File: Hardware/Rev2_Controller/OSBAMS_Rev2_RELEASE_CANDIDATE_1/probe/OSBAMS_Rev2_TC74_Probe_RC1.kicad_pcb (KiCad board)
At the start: 2 copper layers, 30 x 18 mm, 5 parts, among them J1 TO_CONTROLLER, U1 TC74A5-3.3VAT

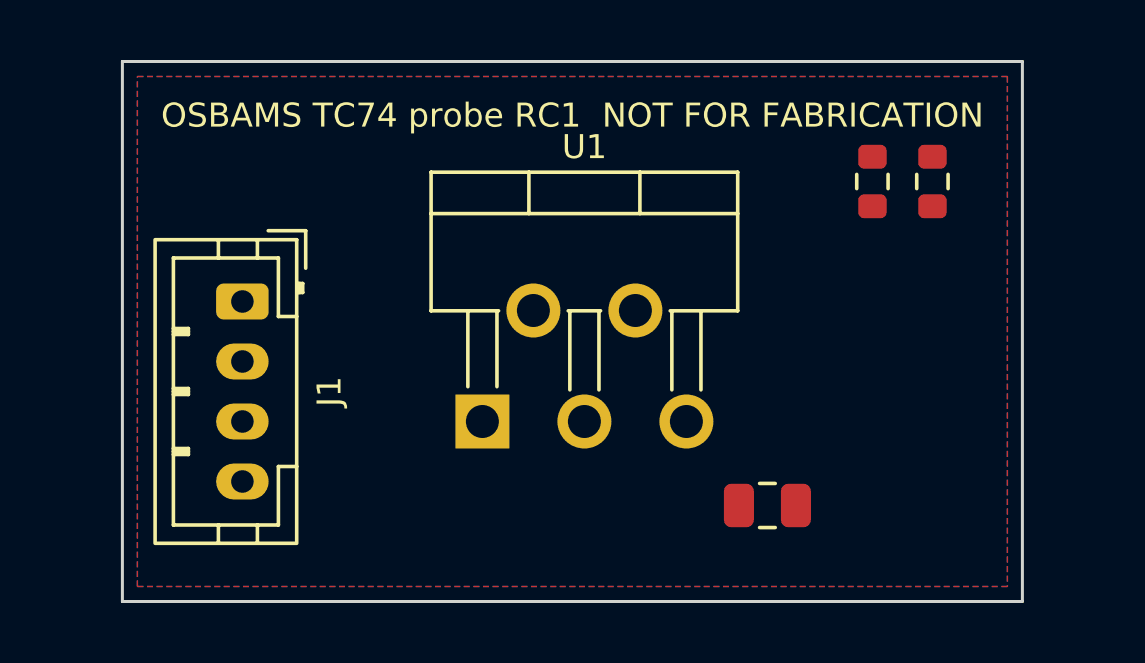
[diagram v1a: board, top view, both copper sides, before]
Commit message: RC1: reconcile user-relayed manufacturer data (USER_RELAYED_MANUFACTURER)
- audit report MANUFACTURER_DATA_RECONCILIATION.md; INA228/STM32/IRLML0060/LMR14006Y/CP2102N/VO610A/TC74 pin maps match the relayed data
- ISO7721 pin-direction conflict left unresolved (needs the TI pin diagram); CP2102N VBUS reference connection open
- LMR14006Y: 95 ns TON_MIN analysis (15 V marginal, 24.4 V below TON_MIN); 1.5SMBJ48A vs INA228 85 V clamp-vs-current analysis
- firmware: INA228 IMAX 30 A -> 20 A (SHUNT_CAL 1250) + test
- fix: TC74 probe PCB had been left unrouted by the schematic step; re-routed, DRC 0; schematic step no longer rebuilds it

Co-Authored-By: Claude Sonnet 5.5 <noreply@anthropic.com>
Claude-Session: https://claude.ai/code/session_01HV1TCrYnLTcNjmYdFqCPLo
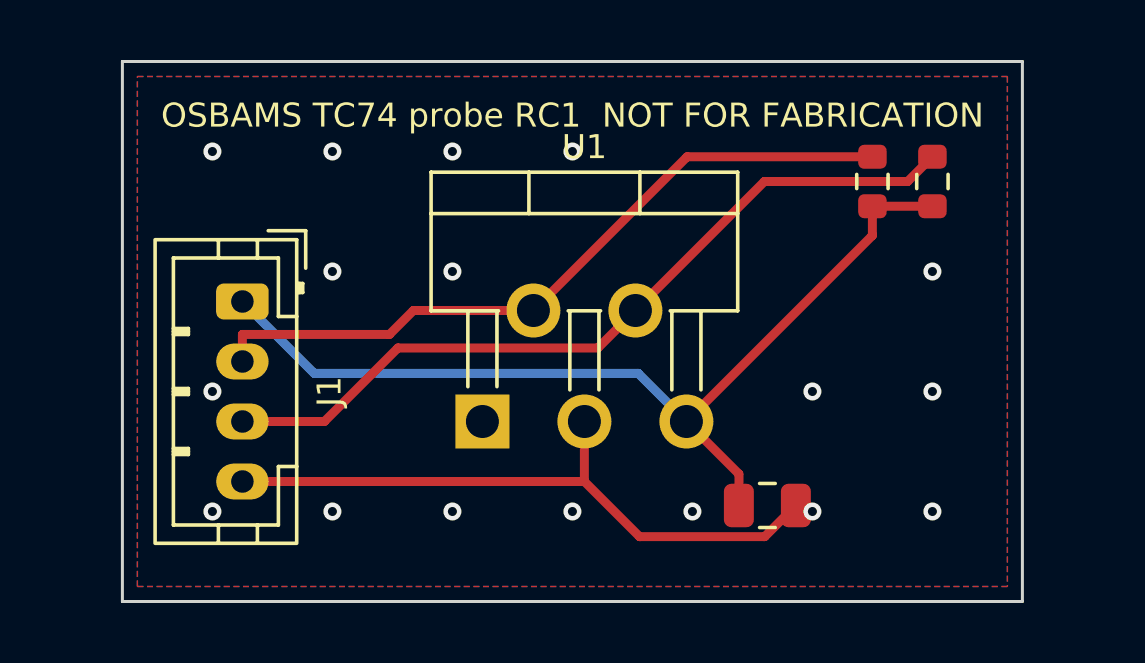
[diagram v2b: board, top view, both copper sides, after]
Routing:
- net +3V3: track 0.00 -> 31.7 mm
- net SCL: track 0.00 -> 26.7 mm
- net SDA: track 0.00 -> 24.4 mm
- net GND: track 0.00 -> 21.6 mm, vias 0 -> 17
